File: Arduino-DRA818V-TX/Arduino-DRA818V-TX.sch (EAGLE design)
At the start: 22 parts, among them M1 ARDUINO_R3_ICSP, X1 SMA, X2 SMA

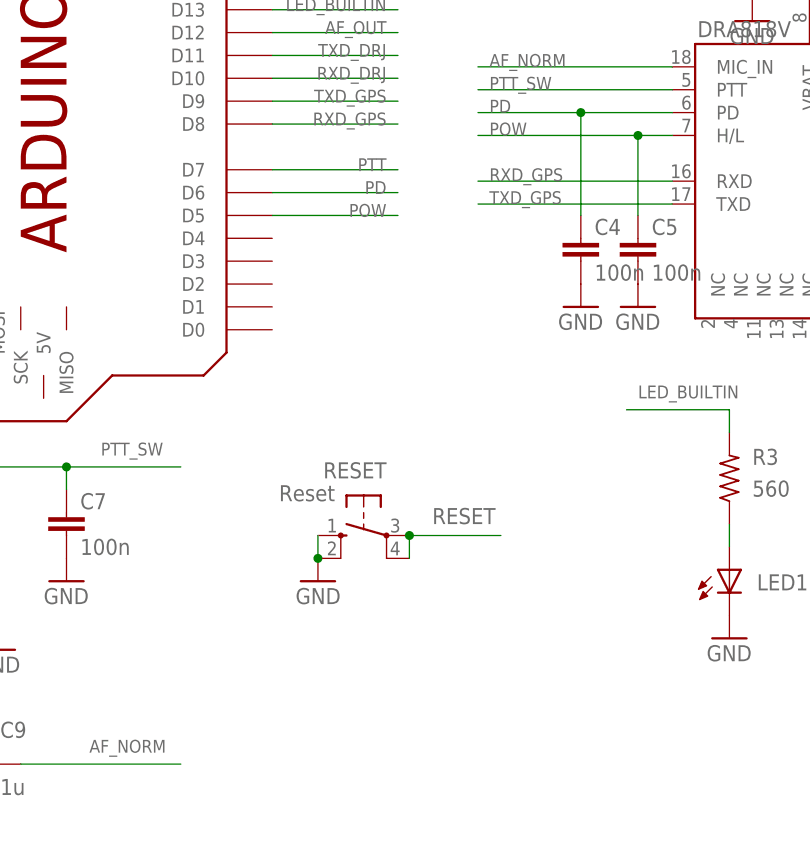
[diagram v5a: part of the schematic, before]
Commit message: Adding GPS Port
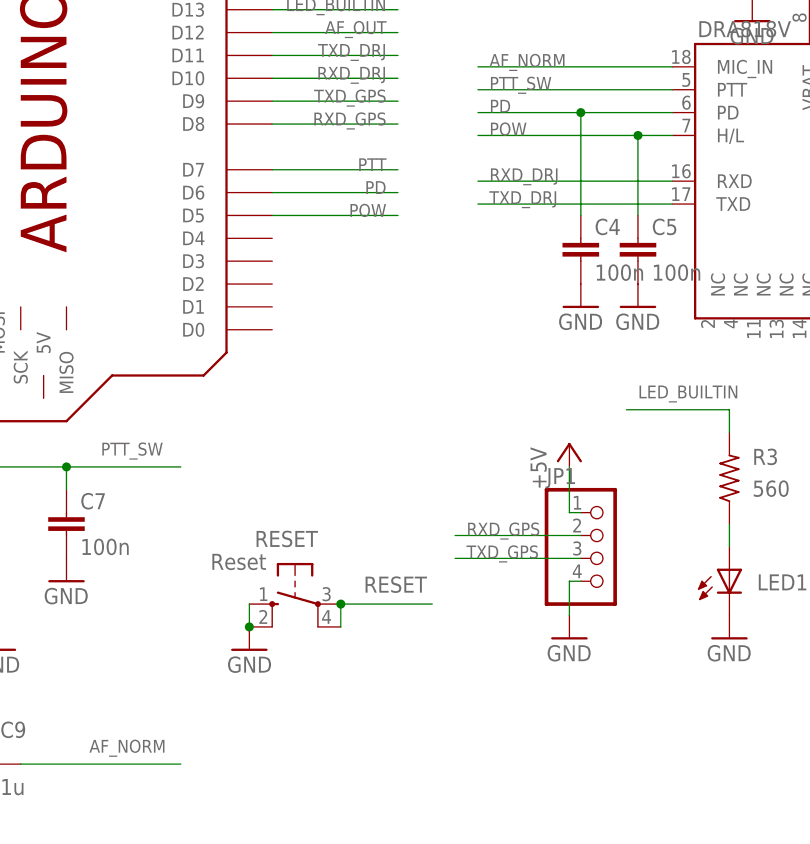
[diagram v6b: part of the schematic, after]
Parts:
- added JP1: (no value), pinhead:PINHD-1X4
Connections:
- net +5V: now also JP1.1
- net GND: now also JP1.4
- net RXD_DRJ: now also DRA818V.RXD
- net RXD_GPS: now also JP1.2; no longer DRA818V.RXD
- net TXD_DRJ: now also DRA818V.TXD
- net TXD_GPS: now also JP1.3; no longer DRA818V.TXD
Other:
- moved on the sheet: RESET
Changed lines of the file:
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@@
 <part name="C10" library="resistor" deviceset="C-EU" device="C1206" value="1n"/>
 <part name="GND20" library="supply1" deviceset="GND" device=""/>
+<part name="JP1" library="pinhead" deviceset="PINHD-1X4" device=""/>
+<part name="P+4" library="supply1" deviceset="+5V" device=""/>
+<part name="GND21" library="supply1" deviceset="GND" device=""/>
 </parts>
 <sheets>
@@
 </plain>
 <instances>
-<instance part="RESET" gate="1" x="91.44" y="49.53" rot="MR270"/>
+<instance part="RESET" gate="1" x="83.82" y="41.91" rot="MR270"/>
 <instance part="P+1" gate="1" x="140.97" y="124.46"/>
-<instance part="GND2" gate="1" x="86.36" y="44.45" rot="MR0"/>
+<instance part="GND2" gate="1" x="78.74" y="36.83" rot="MR0"/>
 <instance part="GND4" gate="1" x="132.08" y="38.1"/>
 <instance part="LED1" gate="G$1" x="132.08" y="45.72" smashed="yes">
@@
 <instance part="C10" gate="G$1" x="134.62" y="114.3"/>
 <instance part="GND20" gate="1" x="134.62" y="106.68"/>
+<instance part="JP1" gate="A" x="118.11" y="46.99"/>
+<instance part="P+4" gate="1" x="114.3" y="59.69"/>
+<instance part="GND21" gate="1" x="114.3" y="38.1"/>
 </instances>
 <busses>
@@
 <wire x1="147.32" y1="63.5" x2="147.32" y2="60.96" width="0.1524" layer="91"/>
 </segment>
+<segment>
+<pinref part="JP1" gate="A" pin="1"/>
+<pinref part="P+4" gate="1" pin="+5V"/>
+<wire x1="115.57" y1="52.07" x2="114.3" y2="52.07" width="0.1524" layer="91"/>
+<wire x1="114.3" y1="52.07" x2="114.3" y2="57.15" width="0.1524" layer="91"/>
+</segment>
 </net>
 <net name="GND" class="0">
 <segment>
-<wire x1="86.36" y1="49.53" x2="86.36" y2="46.99" width="0.1524" layer="91"/>
-<junction x="86.36" y="46.99"/>
+<wire x1="78.74" y1="41.91" x2="78.74" y2="39.37" width="0.1524" layer="91"/>
+<junction x="78.74" y="39.37"/>
 <pinref part="RESET" gate="1" pin="S"/>
 <pinref part="RESET" gate="1" pin="S1"/>
@@
 <pinref part="GND20" gate="1" pin="GND"/>
 </segment>
+<segment>
+<pinref part="JP1" gate="A" pin="4"/>
+<pinref part="GND21" gate="1" pin="GND"/>
+<wire x1="115.57" y1="44.45" x2="114.3" y2="44.45" width="0.1524" layer="91"/>
+<wire x1="114.3" y1="44.45" x2="114.3" y2="40.64" width="0.1524" layer="91"/>
+</segment>
 </net>
 <net name="RESET" class="0">
 <segment>
-<wire x1="96.52" y1="46.99" x2="96.52" y2="49.53" width="0.1524" layer="91"/>
-<wire x1="96.52" y1="49.53" x2="106.68" y2="49.53" width="0.1524" layer="91"/>
-<junction x="96.52" y="49.53"/>
+<wire x1="88.9" y1="39.37" x2="88.9" y2="41.91" width="0.1524" layer="91"/>
+<wire x1="88.9" y1="41.91" x2="99.06" y2="41.91" width="0.1524" layer="91"/>
+<junction x="88.9" y="41.91"/>
 <pinref part="RESET" gate="1" pin="P"/>
 <pinref part="RESET" gate="1" pin="P1"/>
-<label x="99.06" y="50.8" size="1.778" layer="95"/>
+<label x="91.44" y="43.18" size="1.778" layer="95"/>
 </segment>
 <segment>
@@
 <label x="93.98" y="104.14" size="1.4224" layer="95" rot="R180"/>
 </segment>
+<segment>
+<pinref part="DRA818V" gate="G$1" pin="TXD"/>
+<wire x1="125.73" y1="86.36" x2="104.14" y2="86.36" width="0.1524" layer="91"/>
+<label x="105.41" y="86.36" size="1.4224" layer="95"/>
+</segment>
 </net>
 <net name="RXD_DRJ" class="0">
@@
 <label x="93.98" y="101.6" size="1.4224" layer="95" rot="R180"/>
 </segment>
+<segment>
+<pinref part="DRA818V" gate="G$1" pin="RXD"/>
+<wire x1="125.73" y1="88.9" x2="104.14" y2="88.9" width="0.1524" layer="91"/>
+<label x="105.41" y="88.9" size="1.4224" layer="95"/>
+</segment>
 </net>
 <net name="TXD_GPS" class="0">
@@
 </segment>
 <segment>
-<pinref part="DRA818V" gate="G$1" pin="TXD"/>
-<wire x1="125.73" y1="86.36" x2="104.14" y2="86.36" width="0.1524" layer="91"/>
-<label x="105.41" y="86.36" size="1.4224" layer="95"/>
+<pinref part="JP1" gate="A" pin="3"/>
+<wire x1="115.57" y1="46.99" x2="101.6" y2="46.99" width="0.1524" layer="91"/>
+<label x="102.87" y="46.99" size="1.4224" layer="95"/>
 </segment>
 </net>
@@
 </segment>
 <segment>
-<pinref part="DRA818V" gate="G$1" pin="RXD"/>
-<wire x1="125.73" y1="88.9" x2="104.14" y2="88.9" width="0.1524" layer="91"/>
-<label x="105.41" y="88.9" size="1.4224" layer="95"/>
-</segment>
-</net>
+<pinref part="JP1" gate="A" pin="2"/>
+<wire x1="115.57" y1="49.53" x2="101.6" y2="49.53" width="0.1524" layer="91"/>
+<label x="102.87" y="49.53" size="1.4224" layer="95"/>
+</segment>
+</net>
